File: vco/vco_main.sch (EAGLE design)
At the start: 101 parts, among them IC1 OPA4130U, IC2 LM13700M, IC3 OPA4130U, IC4 OPA4130U, Q1 MMBFJ3

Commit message: changed a bunch of stuff.
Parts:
- renumbered SYNCSW to S1
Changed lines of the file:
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@@
 <part name="GND30" library="dan" deviceset="GND" device=""/>
 <part name="GND31" library="dan" deviceset="GND" device=""/>
-<part name="SYNCSW" library="dan" deviceset="255SB" device=""/>
 <part name="R47" library="dan" deviceset="R-US_" device="R0603" value="4.7K"/>
 <part name="GND32" library="dan" deviceset="GND" device=""/>
@@
 <part name="R53" library="dan" deviceset="R-US_" device="R0603" value="20k"/>
 <part name="LED1" library="dan" deviceset="LED" device="5MM"/>
+<part name="S1" library="dan" deviceset="255SB" device=""/>
 </parts>
 <sheets>
@@
 <instance part="GND30" gate="1" x="223.52" y="129.54" rot="MR0"/>
 <instance part="GND31" gate="1" x="259.08" y="132.08" rot="MR0"/>
-<instance part="SYNCSW" gate="1" x="187.96" y="142.24" rot="R270"/>
 <instance part="R47" gate="G$1" x="119.38" y="0" rot="MR270"/>
 <instance part="GND32" gate="1" x="119.38" y="-10.16" rot="MR0"/>
@@
 <instance part="R53" gate="G$1" x="60.96" y="-22.86" rot="MR90"/>
 <instance part="LED1" gate="G$1" x="119.38" y="12.7" rot="R180"/>
+<instance part="S1" gate="1" x="187.96" y="142.24" rot="R270"/>
 </instances>
 <busses>
@@
 </segment>
 <segment>
-<pinref part="SYNCSW" gate="1" pin="P"/>
 <wire x1="182.88" y1="139.7" x2="175.26" y2="139.7" width="0.1524" layer="91"/>
 <label x="175.26" y="139.7" size="1.778" layer="95"/>
+<pinref part="S1" gate="1" pin="P"/>
 </segment>
 </net>
@@
 <segment>
 <pinref part="C7" gate="G$1" pin="2"/>
-<pinref part="SYNCSW" gate="1" pin="S"/>
 <wire x1="195.58" y1="137.16" x2="193.04" y2="137.16" width="0.1524" layer="91"/>
-</segment>
-</net>
+<pinref part="S1" gate="1" pin="S"/>
+</segment>
+</net>

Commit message: almost done with the filter board
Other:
- note removed: "C11 is close to a via, but I'm not sure whether to work on that one or not."
- note removed: "Moved via away from R25 to prevent a short when assembling"
- note removed: "Moved vias away from C10, C14, C5 and C1."
- note removed: "Need to either change switch footprint or find a different switch."
- note removed: "Post Fab Notes:"
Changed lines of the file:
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@@
 <plain>
 <text x="165.1" y="132.08" size="1.778" layer="91">Verify location of sync input</text>
-<text x="-121.92" y="154.94" size="1.778" layer="91">Post Fab Notes:</text>
-<text x="-121.92" y="149.86" size="1.778" layer="91">Moved via away from R25 to prevent a short when assembling</text>
-<text x="-121.92" y="144.78" size="1.778" layer="91">Need to either change switch footprint or find a different switch.</text>
-<text x="-121.92" y="139.7" size="1.778" layer="91">Moved vias away from C10, C14, C5 and C1.</text>
-<text x="-121.92" y="134.62" size="1.778" layer="91">C11 is close to a via, but I'm not sure whether to work on that one or not.</text>
 </plain>
 <instances>

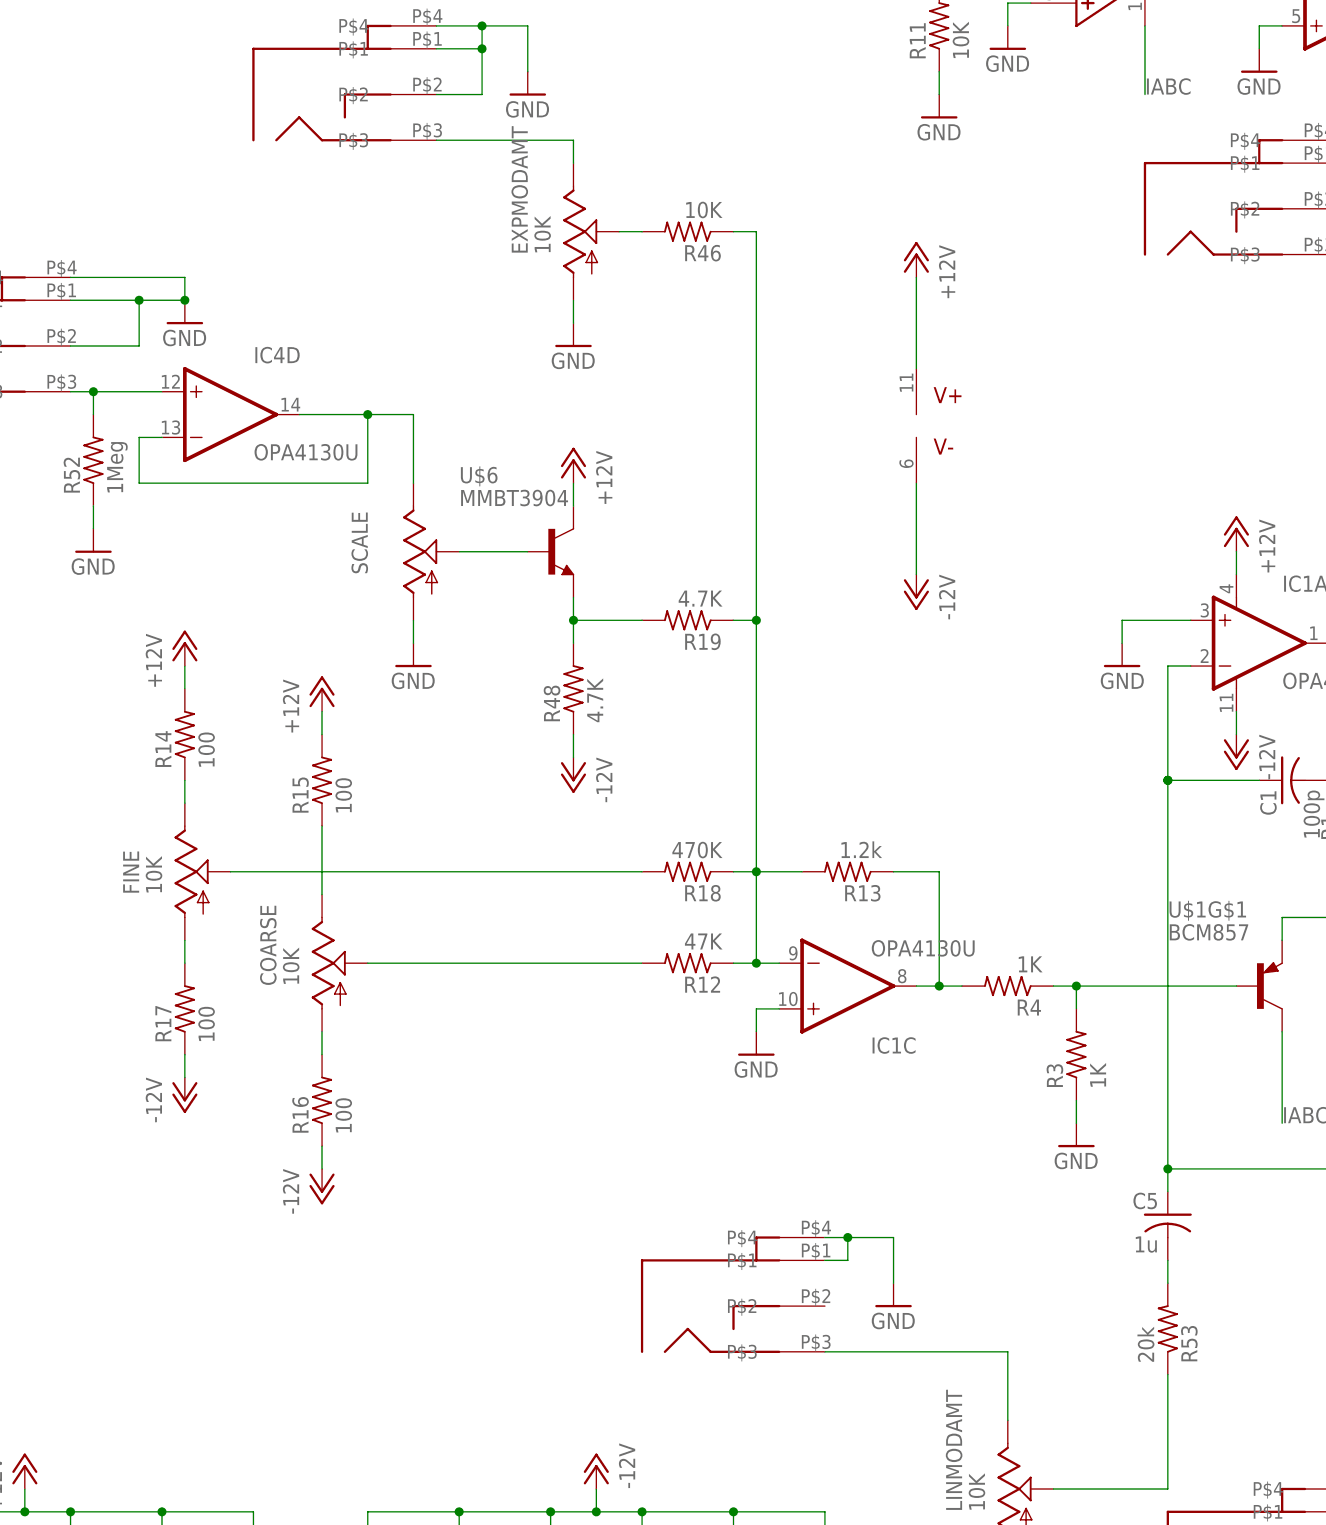
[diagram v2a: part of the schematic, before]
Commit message: added 2 board rev of the vcf in a separate folder
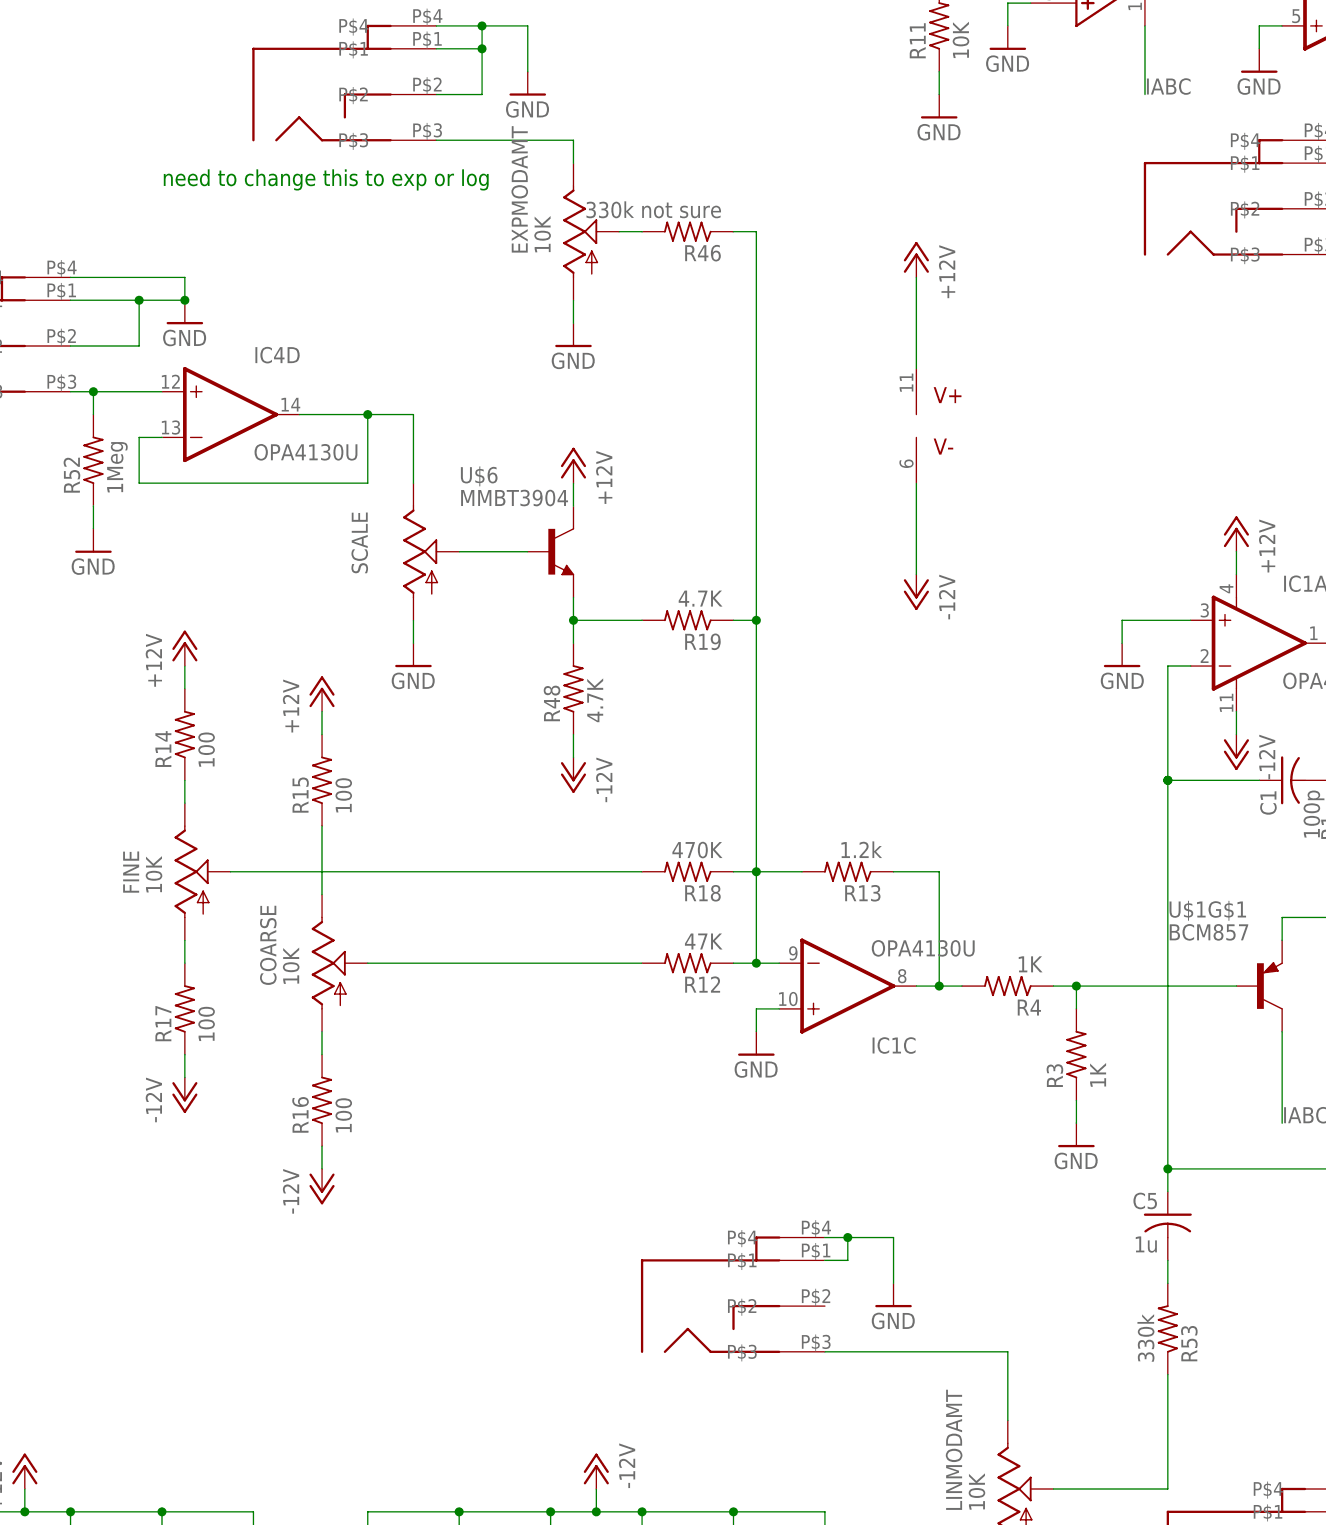
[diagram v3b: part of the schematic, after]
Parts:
- R46: value 10K -> 330k not sure
- R53: value 20k -> 330k
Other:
- note added: "need to change this to exp or log"
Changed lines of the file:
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@@
 <part name="R45" library="dan" deviceset="R-US_" device="R0603" value="10K"/>
 <part name="GND25" library="dan" deviceset="GND" device=""/>
-<part name="R46" library="dan" deviceset="R-US_" device="R0603" value="10K"/>
+<part name="R46" library="dan" deviceset="R-US_" device="R0603" value="330k not sure"/>
 <part name="EXPMODAMT" library="dan" deviceset="US-EVU" device="F2J" value="10K"/>
 <part name="GND26" library="dan" deviceset="GND" device=""/>
@@
 <part name="GND37" library="dan" deviceset="GND" device=""/>
 <part name="GND38" library="dan" deviceset="GND" device=""/>
-<part name="R53" library="dan" deviceset="R-US_" device="R0603" value="20k"/>
+<part name="R53" library="dan" deviceset="R-US_" device="R0603" value="330k"/>
 <part name="LED1" library="dan" deviceset="LED" device="5MM"/>
 <part name="S1" library="dan" deviceset="255SB" device=""/>
@@
 <plain>
 <text x="165.1" y="132.08" size="1.778" layer="91">Verify location of sync input</text>
+<text x="-50.8" y="104.14" size="1.778" layer="91">need to change this to exp or log</text>
 </plain>
 <instances>
